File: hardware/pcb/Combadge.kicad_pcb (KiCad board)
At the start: 2 copper layers, 34.5 x 31 mm, 27 parts, among them J1 Conn_01x05_Female, J2 USB_B_Micro, J3 TOUCH, U1 XC6808A4D28R-G, U2 ESP32-WROOM-32, U3 NCP160AMX330TBG, U4 NAU8315YG

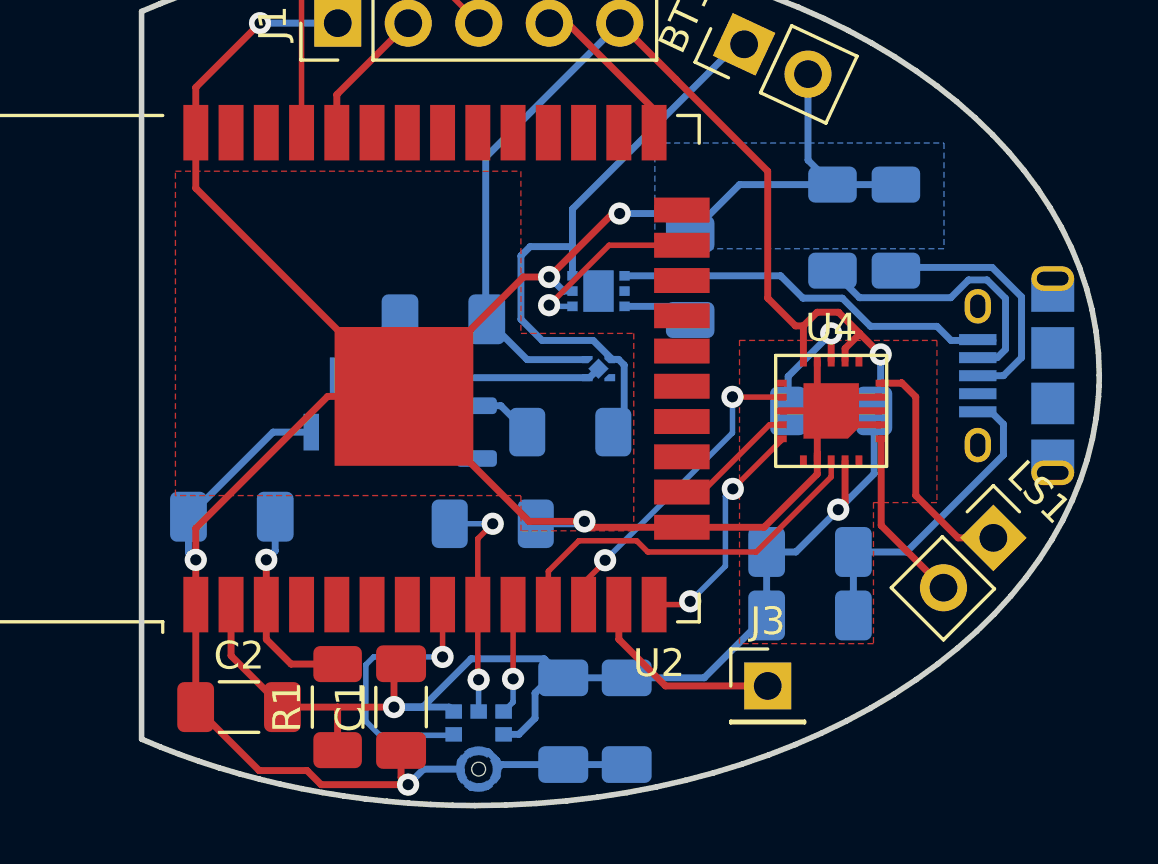
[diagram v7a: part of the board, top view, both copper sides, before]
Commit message: Fix some DRC errors
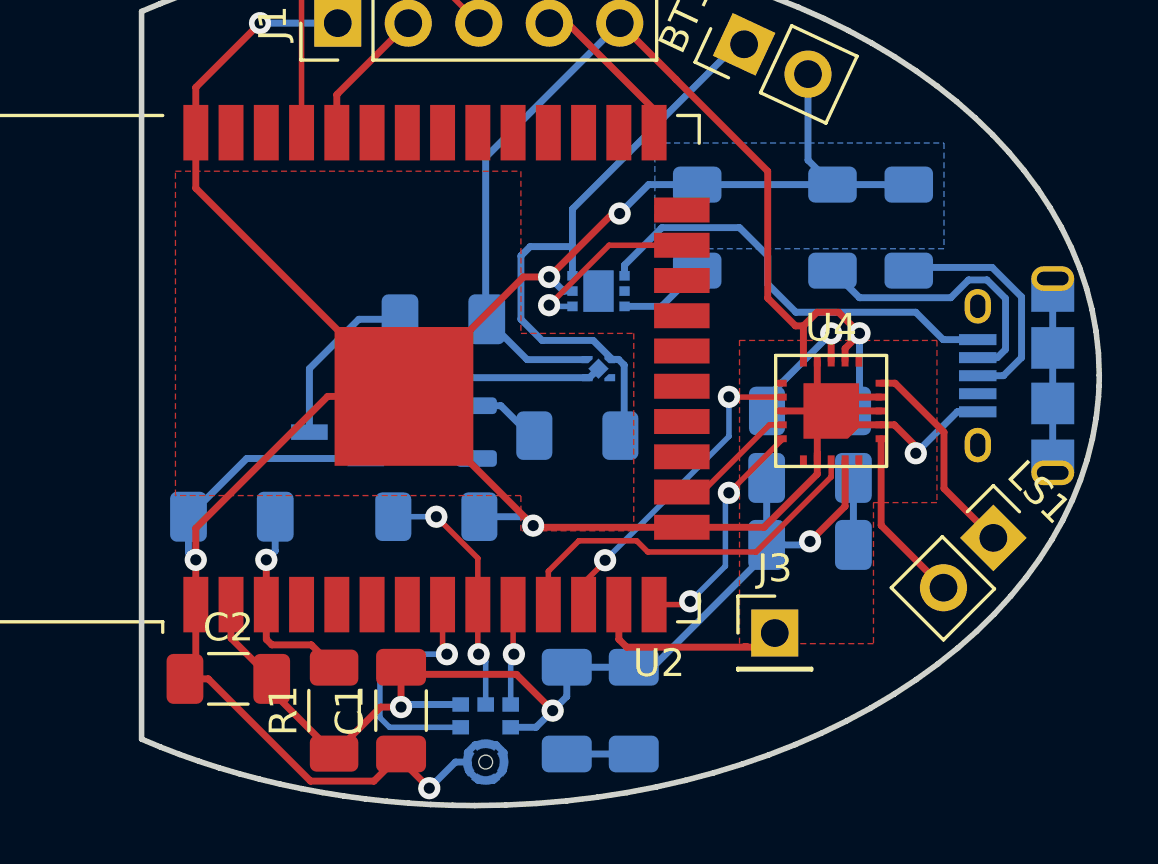
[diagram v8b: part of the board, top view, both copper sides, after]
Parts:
- MOSFET1: value SI2342DS-T1-GE3 -> SI2342DS
- moved C6 2.67 mm to (87.1, 64.9)
- moved C5 2.54 mm to (87.1, 67.3)
- moved R6 2.05 mm to (73.7, 66.3)
- moved J3 1.92 mm to (85.9, 70.5)
- moved R_ISET1 1.80 mm to (83.1, 55.9)
- moved C2 1.09 mm to (66.2, 72.1)
- moved MOSFET1 1.02 mm to (70.1, 63.2), turned to -90 degrees
- moved R5 0.76 mm to (87.1, 62.5)
- moved R2 0.46 mm to (90.7, 55.9)
- moved C8 0.46 mm to (80.8, 73.3)
- moved C7 0.40 mm to (78.4, 73.3)
- moved MK1 0.36 mm to (75.4, 74.4)
- moved R4 0.28 mm to (78.7, 63.4)
- moved R1 0.18 mm to (70.0, 73.3)
- moved C1 0.13 mm to (72.4, 73.3)
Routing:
- net unconnected-(J2-Pad6): track 0.00 -> 7.00 mm
- net GND: track 131.4 -> 127.1 mm, vias 6 -> 7
- net Net-(C4-Pad2): track 11.0 -> 14.4 mm
- net +3.3V: track 81.6 -> 78.3 mm, vias 3 -> 4
- net Net-(J2-Pad1): track 14.2 -> 15.9 mm
- net Net-(R_ISET1-Pad2): track 1.87 -> 3.15 mm
- net Net-(LS1-Pad1): track 8.45 -> 7.54 mm
- net /MIC_BCLK: track 10.1 -> 9.38 mm
- net /MIC_SD: track 8.55 -> 9.05 mm
